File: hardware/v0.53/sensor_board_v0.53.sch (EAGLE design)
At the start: 55 parts, among them J3 USB-MICROB, U1 ATMEGA328P, U10 TSL2591, U3 OPA344, U4 RFM69HW, U5 FT231XS, U6 ADMP401, U7 SHT31-DIS, U8 MCP1703CB, U9 BMP280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

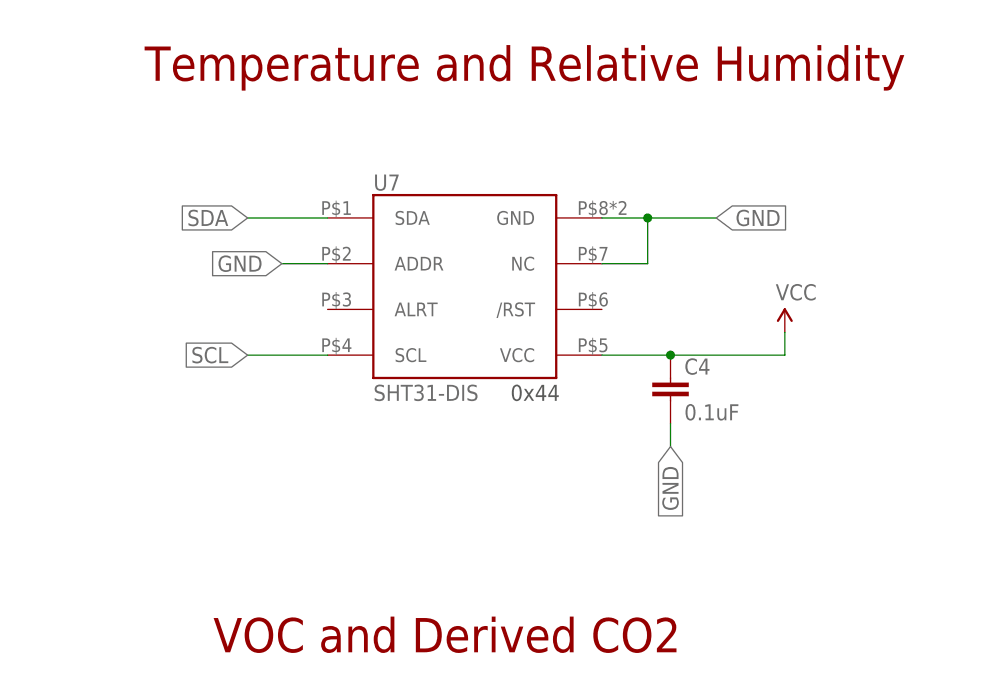
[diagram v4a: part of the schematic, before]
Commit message: Updated SHT31/35 library
Replaced old library with Adafruit version - slightly longer pads to avoid potential bridging during reflow.
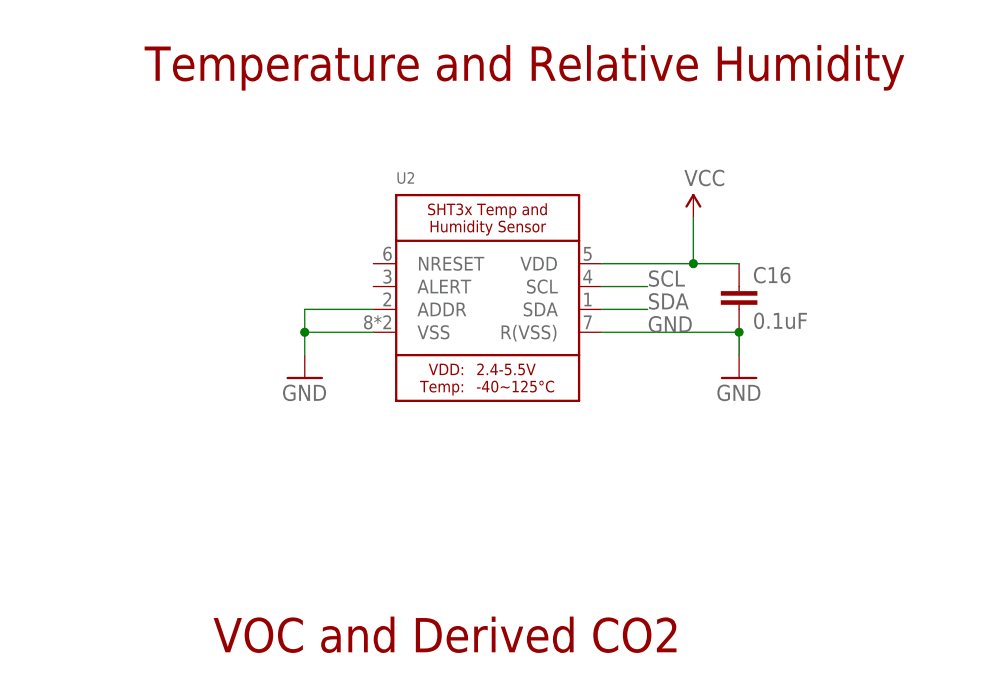
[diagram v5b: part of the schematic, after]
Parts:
- removed C4: 0.1uF, SparkFun-Passives:CAP0805
- removed U7: SHT31-DIS, thomasb9511:SHT31-DIS
- added C16: 0.1uF, SparkFun-Passives:CAP0805
- added U2: (no value), Adafruit SHT31:SHT3X
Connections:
- net GND: now also C16.2, U2.ADDR, U2.R(VSS), U2.VSS; no longer C4.2, U7.ADDR, U7.GND, U7.NC
- net SCL: now also U2.SCL; no longer U7.SCL
- net SDA: now also U2.SDA; no longer U7.SDA
- net VCC: now also C16.1, U2.VDD; no longer C4.1, U7.VCC
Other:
- note removed: "0x44"
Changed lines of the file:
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@@
 <attribute name="OC_NEWARK" value="58Y6083"/>
-</part>
-<part name="U7" library="thomasb9511" deviceset="SHT31-DIS" device="">
-<attribute name="MF" value=""/>
-<attribute name="MPN" value="SHT31-DIS-B"/>
-<attribute name="OC_NEWARK" value="47Y1304"/>
 </part>
 <part name="IAQ-CORE" library="IAQ-CORE" deviceset="IAQ-CORE" device="">
@@
 <part name="GND1" library="SparkFun-Aesthetics" deviceset="GND" device=""/>
 <part name="SUPPLY1" library="SparkFun-Aesthetics" deviceset="VCC" device=""/>
-<part name="SUPPLY3" library="SparkFun-Aesthetics" deviceset="VCC" device=""/>
 <part name="SUPPLY5" library="SparkFun-Aesthetics" deviceset="VCC" device=""/>
 <part name="R5" library="SparkFun-Resistors" deviceset="RESISTOR" device="0805-RES" value="10K">
@@
 <part name="R6" library="SparkFun-Resistors" deviceset="RESISTOR" device="0805-RES" value="10K">
 <attribute name="MPN" value="RC0805FR-0710KL"/>
-</part>
-<part name="C4" library="SparkFun-Passives" deviceset="CAP" device="0805" value="0.1uF">
-<attribute name="MPN" value="CC0805KRX7R9BB104"/>
 </part>
 <part name="C5" library="SparkFun-Passives" deviceset="CAP" device="0805" value="0.1uF">
@@
 <part name="J4" library="SparkFun-Connectors" deviceset="M02" device="PTH"/>
 <part name="J5" library="SparkFun-Connectors" deviceset="M02" device="PTH"/>
+<part name="U2" library="Adafruit SHT31" deviceset="SHT3X" device=""/>
+<part name="C16" library="SparkFun-Passives" deviceset="CAP" device="0805" value="0.1uF">
+<attribute name="MPN" value="CC0805KRX7R9BB104"/>
+</part>
+<part name="SUPPLY2" library="SparkFun-Aesthetics" deviceset="VCC" device=""/>
+<part name="GND8" library="SparkFun-Aesthetics" deviceset="GND" device=""/>
+<part name="GND13" library="SparkFun-Aesthetics" deviceset="GND" device=""/>
 </parts>
 <sheets>
@@
 <text x="-55.88" y="-45.72" size="3.81" layer="94">USB + FTDI</text>
 <text x="246.38" y="-78.74" size="1.778" layer="97">0x5A</text>
-<text x="248.92" y="-5.08" size="1.778" layer="97">0x44</text>
 <text x="157.48" y="12.7" size="1.778" layer="97">0x77</text>
 <text x="257.556" y="-102.362" size="2.54" layer="94" font="vector" ratio="10">0.53</text>
@@
 <attribute name="MPN" x="238.76" y="81.28" size="1.778" layer="96" rot="R270" display="off"/>
 </instance>
-<instance part="U7" gate="G$1" x="243.84" y="7.62">
-<attribute name="OC_NEWARK" x="243.84" y="7.62" size="1.778" layer="96" rot="R270" display="off"/>
-<attribute name="MF" x="243.84" y="7.62" size="1.778" layer="96" rot="R270" display="off"/>
-<attribute name="MPN" x="243.84" y="7.62" size="1.778" layer="96" rot="R270" display="off"/>
-</instance>
 <instance part="IAQ-CORE" gate="G$1" x="238.76" y="-59.69">
 <attribute name="OC_NEWARK" x="238.76" y="-59.69" size="1.778" layer="96" rot="R270" display="off"/>
@@
 <instance part="GND1" gate="1" x="208.28" y="48.26"/>
 <instance part="SUPPLY1" gate="G$1" x="208.28" y="127"/>
-<instance part="SUPPLY3" gate="G$1" x="279.4" y="2.54"/>
 <instance part="SUPPLY5" gate="G$1" x="269.24" y="-50.8"/>
 <instance part="R5" gate="G$1" x="274.32" y="109.22" rot="R90">
@@
 <instance part="R6" gate="G$1" x="284.48" y="109.22" rot="R90">
 <attribute name="MPN" x="284.48" y="109.22" size="1.778" layer="96" rot="R90" display="off"/>
-</instance>
-<instance part="C4" gate="G$1" x="266.7" y="-5.08">
-<attribute name="MPN" x="266.7" y="-5.08" size="1.778" layer="96" rot="R270" display="off"/>
 </instance>
 <instance part="C5" gate="G$1" x="269.24" y="-60.96">
@@
 <instance part="J4" gate="G$1" x="-10.16" y="-12.7"/>
 <instance part="J5" gate="G$1" x="20.32" y="-12.7"/>
+<instance part="U2" gate="G$1" x="246.38" y="7.62"/>
+<instance part="C16" gate="G$1" x="274.32" y="5.08">
+<attribute name="MPN" x="274.32" y="5.08" size="1.778" layer="96" rot="R270" display="off"/>
+</instance>
+<instance part="SUPPLY2" gate="G$1" x="269.24" y="15.24"/>
+<instance part="GND8" gate="1" x="274.32" y="-2.54"/>
+<instance part="GND13" gate="1" x="226.06" y="-2.54"/>
 </instances>
 <busses>
@@
 </segment>
 <segment>
-<pinref part="C4" gate="G$1" pin="2"/>
-<wire x1="266.7" y1="-7.62" x2="266.7" y2="-10.16" width="0.1524" layer="91"/>
-<label x="266.7" y="-10.16" size="1.778" layer="95" rot="R270" xref="yes"/>
-</segment>
-<segment>
-<pinref part="U7" gate="G$1" pin="GND"/>
-<wire x1="259.08" y1="15.24" x2="264.16" y2="15.24" width="0.1524" layer="91"/>
-<label x="271.78" y="15.24" size="1.778" layer="95" xref="yes"/>
-<pinref part="U7" gate="G$1" pin="NC"/>
-<wire x1="264.16" y1="15.24" x2="271.78" y2="15.24" width="0.1524" layer="91"/>
-<wire x1="259.08" y1="10.16" x2="264.16" y2="10.16" width="0.1524" layer="91"/>
-<wire x1="264.16" y1="10.16" x2="264.16" y2="15.24" width="0.1524" layer="91"/>
-<junction x="264.16" y="15.24"/>
-</segment>
-<segment>
-<pinref part="U7" gate="G$1" pin="ADDR"/>
-<wire x1="228.6" y1="10.16" x2="223.52" y2="10.16" width="0.1524" layer="91"/>
-<label x="223.52" y="10.16" size="1.778" layer="95" rot="R180" xref="yes"/>
-</segment>
-<segment>
 <pinref part="U9" gate="G$1" pin="GND"/>
 <wire x1="137.16" y1="17.78" x2="127" y2="17.78" width="0.1524" layer="91"/>
@@
 <wire x1="-2.54" y1="-12.7" x2="0" y2="-12.7" width="0.1524" layer="91"/>
 <label x="0" y="-12.7" size="1.778" layer="95"/>
+</segment>
+<segment>
+<pinref part="C16" gate="G$1" pin="2"/>
+<pinref part="GND8" gate="1" pin="GND"/>
+<wire x1="274.32" y1="2.54" x2="274.32" y2="0" width="0.1524" layer="91"/>
+<pinref part="U2" gate="G$1" pin="R(VSS)"/>
+<label x="264.16" y="2.54" size="1.778" layer="95"/>
+<wire x1="259.08" y1="2.54" x2="274.32" y2="2.54" width="0.1524" layer="91"/>
+<junction x="274.32" y="2.54"/>
+</segment>
+<segment>
+<pinref part="U2" gate="G$1" pin="VSS"/>
+<wire x1="233.68" y1="2.54" x2="226.06" y2="2.54" width="0.1524" layer="91"/>
+<pinref part="GND13" gate="1" pin="GND"/>
+<wire x1="226.06" y1="2.54" x2="226.06" y2="0" width="0.1524" layer="91"/>
+<pinref part="U2" gate="G$1" pin="ADDR"/>
+<wire x1="233.68" y1="5.08" x2="226.06" y2="5.08" width="0.1524" layer="91"/>
+<wire x1="226.06" y1="5.08" x2="226.06" y2="2.54" width="0.1524" layer="91"/>
+<junction x="226.06" y="2.54"/>
 </segment>
 </net>
@@
 </segment>
 <segment>
-<pinref part="U7" gate="G$1" pin="VCC"/>
-<wire x1="259.08" y1="0" x2="266.7" y2="0" width="0.1524" layer="91"/>
-<pinref part="C4" gate="G$1" pin="1"/>
-<pinref part="SUPPLY3" gate="G$1" pin="VCC"/>
-<wire x1="266.7" y1="0" x2="279.4" y2="0" width="0.1524" layer="91"/>
-<wire x1="279.4" y1="0" x2="279.4" y2="2.54" width="0.1524" layer="91"/>
-<junction x="266.7" y="0"/>
-</segment>
-<segment>
 <pinref part="U8" gate="G$1" pin="VO"/>
 <pinref part="C6" gate="G$1" pin="1"/>
@@
 <label x="0" y="-10.16" size="1.778" layer="95"/>
 </segment>
+<segment>
+<pinref part="U2" gate="G$1" pin="VDD"/>
+<pinref part="SUPPLY2" gate="G$1" pin="VCC"/>
+<wire x1="259.08" y1="10.16" x2="269.24" y2="10.16" width="0.1524" layer="91"/>
+<wire x1="269.24" y1="10.16" x2="269.24" y2="15.24" width="0.1524" layer="91"/>
+<pinref part="C16" gate="G$1" pin="1"/>
+<wire x1="269.24" y1="10.16" x2="274.32" y2="10.16" width="0.1524" layer="91"/>
+<junction x="269.24" y="10.16"/>
+</segment>
 </net>
 <net name="SCL" class="0">
@@
 </segment>
 <segment>
-<pinref part="U7" gate="G$1" pin="SCL"/>
-<wire x1="228.6" y1="0" x2="219.71" y2="0" width="0.1524" layer="91"/>
-<label x="219.71" y="0" size="1.778" layer="95" rot="R180" xref="yes"/>
-</segment>
-<segment>
 <pinref part="U9" gate="G$1" pin="SCK"/>
 <wire x1="167.64" y1="22.86" x2="170.18" y2="22.86" width="0.1524" layer="91"/>
@@
 <wire x1="-33.02" y1="-12.7" x2="-30.48" y2="-12.7" width="0.1524" layer="91"/>
 <label x="-30.48" y="-12.7" size="1.778" layer="95"/>
+</segment>
+<segment>
+<pinref part="U2" gate="G$1" pin="SCL"/>
+<wire x1="259.08" y1="7.62" x2="264.16" y2="7.62" width="0.1524" layer="91"/>
+<label x="264.16" y="7.62" size="1.778" layer="95"/>
 </segment>
 </net>
@@
 </segment>
 <segment>
-<pinref part="U7" gate="G$1" pin="SDA"/>
-<wire x1="228.6" y1="15.24" x2="219.71" y2="15.24" width="0.1524" layer="91"/>
-<label x="219.71" y="15.24" size="1.778" layer="95" rot="R180" xref="yes"/>
-</segment>
-<segment>
 <pinref part="IAQ-CORE" gate="G$1" pin="SDA"/>
 <wire x1="256.54" y1="-63.5" x2="259.08" y2="-63.5" width="0.1524" layer="91"/>
@@
 <label x="-30.48" y="-10.16" size="1.778" layer="95"/>
 </segment>
+<segment>
+<pinref part="U2" gate="G$1" pin="SDA"/>
+<wire x1="259.08" y1="5.08" x2="264.16" y2="5.08" width="0.1524" layer="91"/>
+<label x="264.16" y="5.08" size="1.778" layer="95"/>
+</segment>
 </net>

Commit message: Updated BOM
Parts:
- U2: MPN (none) -> SHT35-DIS-B
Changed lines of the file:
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@@
 </part>
 <part name="R3" library="SparkFun-Passives" deviceset="RESISTOR" device="0805-RES" value="1.5K">
-<attribute name="MPN" value="RC0805FR-071K5L
-"/>
+<attribute name="MPN" value="RC0805FR-071K5L "/>
 </part>
 <part name="R7" library="SparkFun-Passives" deviceset="RESISTOR" device="0805-RES" value="10K">
@@
 </part>
 <part name="R8" library="SparkFun-Passives" deviceset="RESISTOR" device="0805-RES" value="100K">
-<attribute name="MPN" value="RC0805FR-07100KL
-"/>
+<attribute name="MPN" value="RC0805FR-07100KL "/>
 </part>
 <part name="SUPPLY4" library="SparkFun-Aesthetics" deviceset="VCC" device=""/>
@@
 </part>
 <part name="R9" library="SparkFun-Passives" deviceset="RESISTOR" device="0805-RES" value="47">
-<attribute name="MPN" value="RC0805FR-0747RL
-"/>
+<attribute name="MPN" value="RC0805FR-0747RL "/>
 </part>
 <part name="R10" library="SparkFun-Passives" deviceset="RESISTOR" device="0805-RES" value="47">
-<attribute name="MPN" value="RC0805FR-0747RL
-"/>
+<attribute name="MPN" value="RC0805FR-0747RL "/>
 </part>
 <part name="R11" library="SparkFun-Passives" deviceset="RESISTOR" device="0805-RES" value="SHOTTKY">
@@
 </part>
 <part name="R12" library="SparkFun-Passives" deviceset="RESISTOR" device="0805-RES" value="27">
-<attribute name="MPN" value="RC0805FR-0727RL
-"/>
+<attribute name="MPN" value="RC0805FR-0727RL "/>
 </part>
 <part name="R21" library="SparkFun-Passives" deviceset="RESISTOR" device="0805-RES" value="27">
-<attribute name="MPN" value="RC0805FR-0727RL
-"/>
+<attribute name="MPN" value="RC0805FR-0727RL "/>
 </part>
 <part name="C11" library="SparkFun-Capacitors" deviceset="CAP" device="0805" value="0.1uF">
@@
 <part name="U$3" library="adafruit" deviceset="FIDUCIAL" device=""/>
 <part name="U10" library="TSL2591" deviceset="LIGHT_TSL2591" device="" value="TSL2591">
-<attribute name="MPN" value="TSL25911FN
-"/>
+<attribute name="MPN" value="TSL25911FN "/>
 </part>
 <part name="C14" library="SparkFun-Passives" deviceset="CAP" device="0805" value="0.1uF">
@@
 <part name="SUPPLY14" library="SparkFun-Aesthetics" deviceset="VCC" device=""/>
 <part name="R16" library="adafruit" deviceset="R-US_" device="R0603" value="470">
-<attribute name="MPN" value="RC0805FR-07470RL
-"/>
+<attribute name="MPN" value="RC0805FR-07470RL "/>
 </part>
 <part name="GND11" library="supply1" deviceset="GND" device=""/>
@@
 <part name="J4" library="SparkFun-Connectors" deviceset="M02" device="PTH"/>
 <part name="J5" library="SparkFun-Connectors" deviceset="M02" device="PTH"/>
-<part name="U2" library="Adafruit SHT31" deviceset="SHT3X" device=""/>
+<part name="U2" library="Adafruit SHT31" deviceset="SHT3X" device="">
+<attribute name="MPN" value="SHT35-DIS-B"/>
+</part>
 <part name="C16" library="SparkFun-Passives" deviceset="CAP" device="0805" value="0.1uF">
 <attribute name="MPN" value="CC0805KRX7R9BB104"/>
@@
 <instance part="J4" gate="G$1" x="-10.16" y="-12.7"/>
 <instance part="J5" gate="G$1" x="20.32" y="-12.7"/>
-<instance part="U2" gate="G$1" x="246.38" y="7.62"/>
+<instance part="U2" gate="G$1" x="246.38" y="7.62">
+<attribute name="MPN" x="246.38" y="7.62" size="1.778" layer="96" display="off"/>
+</instance>
 <instance part="C16" gate="G$1" x="274.32" y="5.08">
 <attribute name="MPN" x="274.32" y="5.08" size="1.778" layer="96" rot="R270" display="off"/>

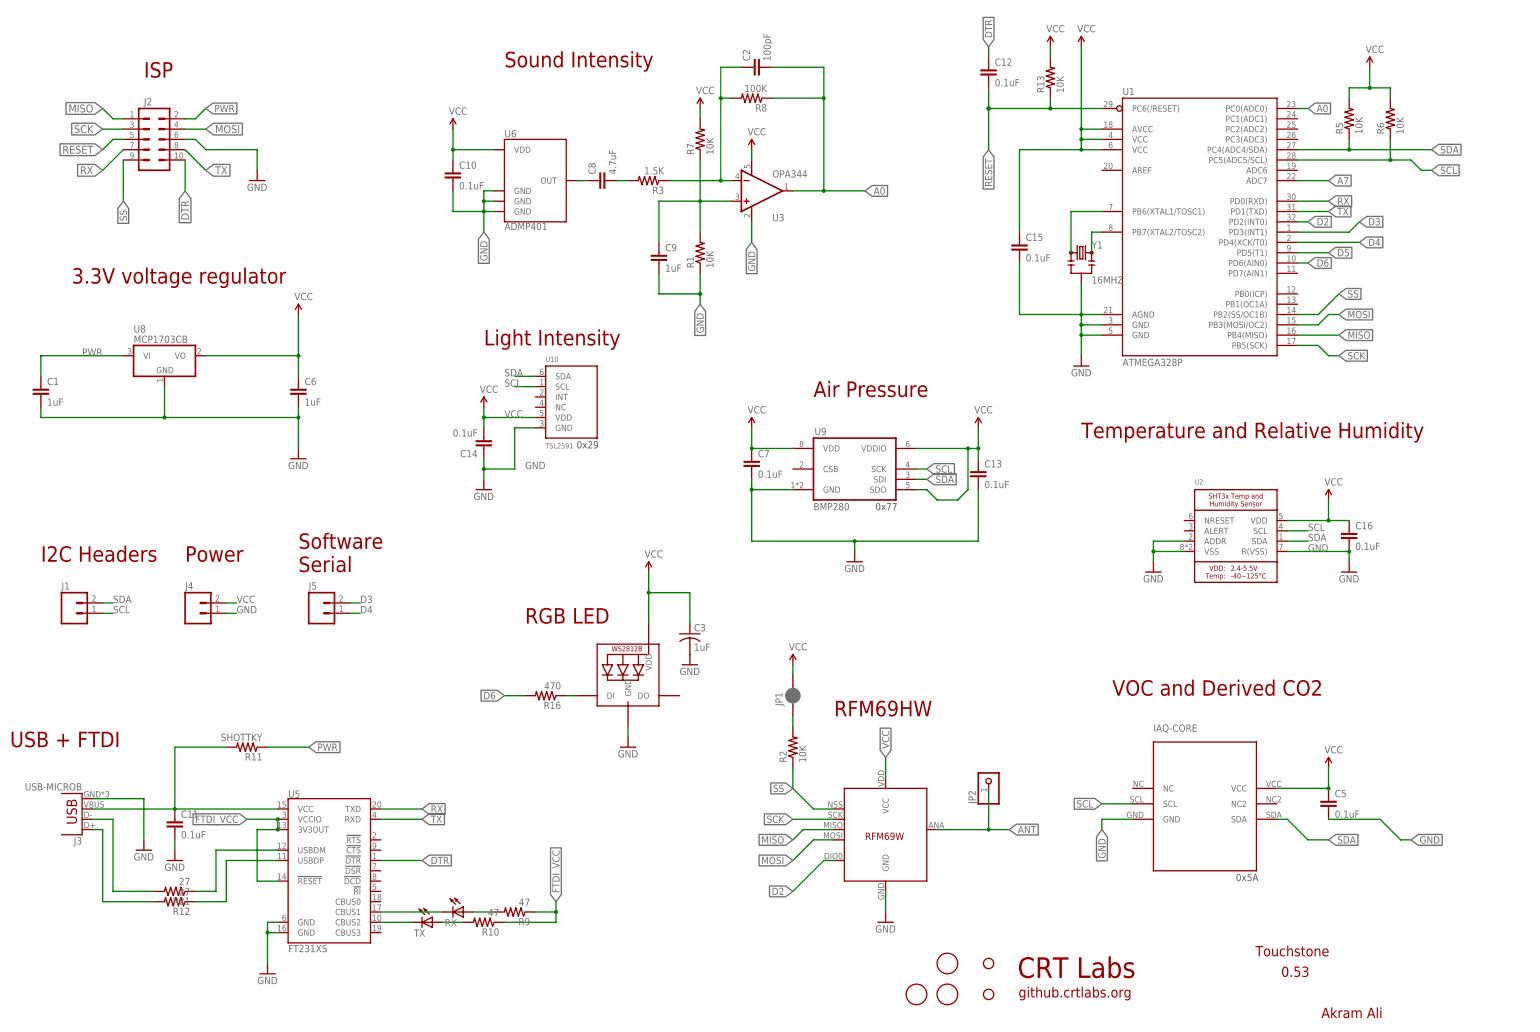
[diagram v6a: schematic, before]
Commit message: v0.53 - update
- Aligned light sensor with RGB LED
- Moved jumpers location after moving light sensor
- Added PM2.5 jumpers (RX/TX/PWR/GND)
- Adjusted some passive components
- Several trace adjustments
- Slightly increased board dimensions for added tolerance on mounting
holes
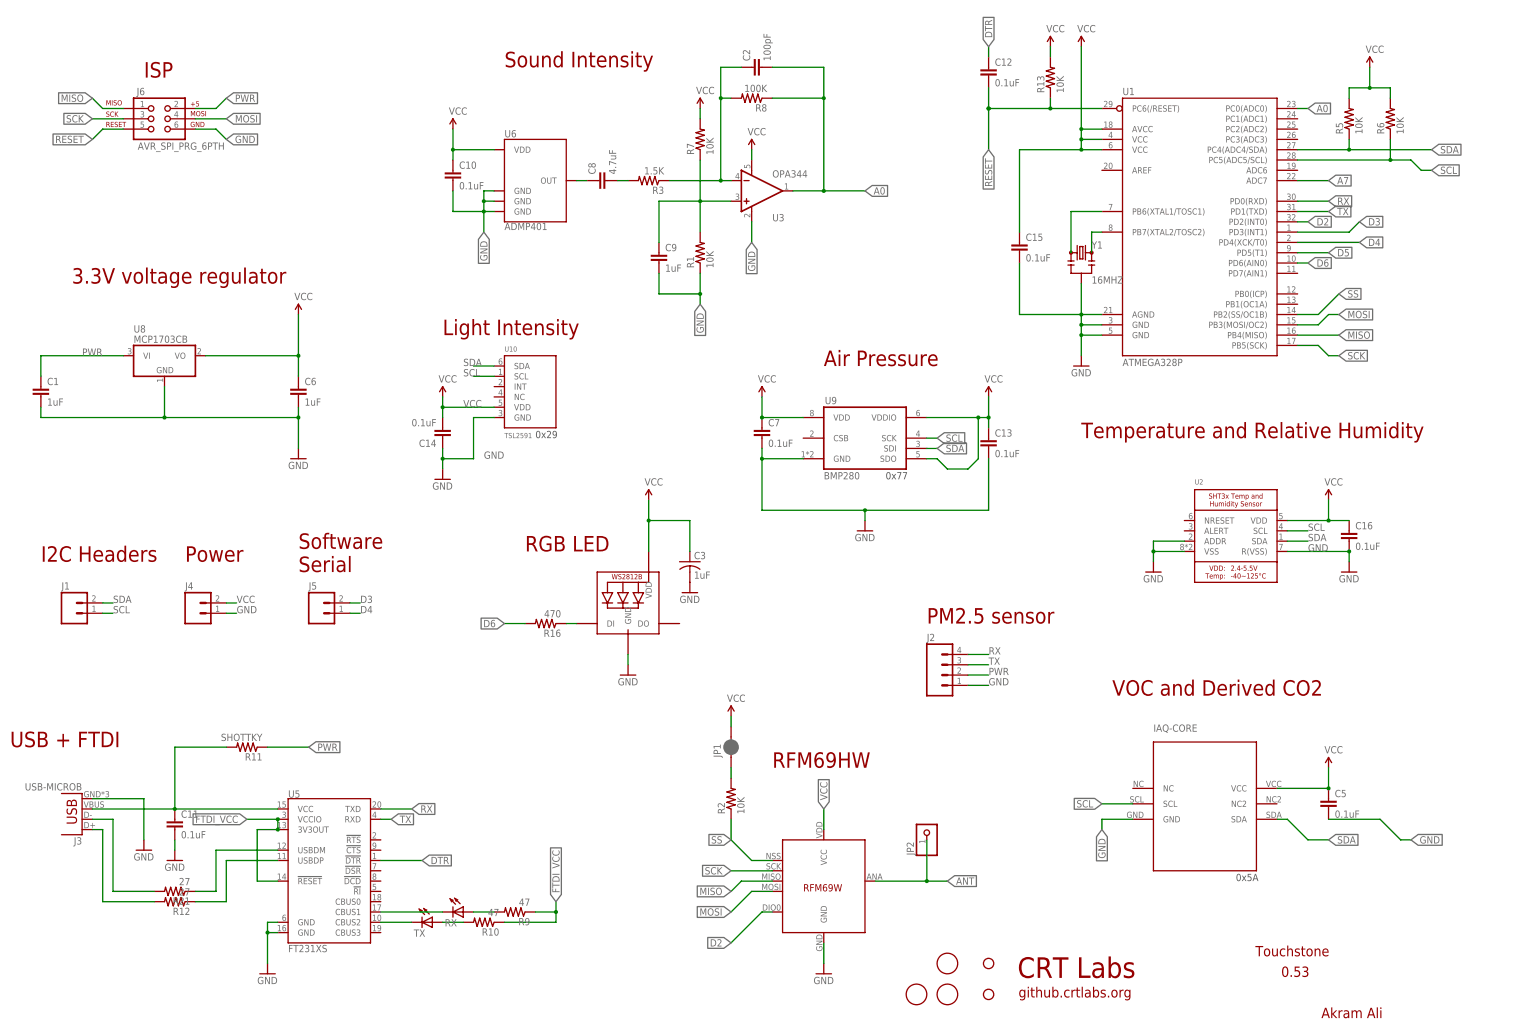
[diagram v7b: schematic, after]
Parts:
- added J6: AVR_SPI_PRG_6PTH, SparkFun-Connectors:AVR_SPI_PRG_6PTH
- J2: device SparkFun-Connectors:M05X2PTH -> SparkFun-Connectors:M04PTH
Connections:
- net DTR: no longer J2.10
- net GND: now also J2.1, J6.6; no longer J2.6
- net MISO: now also J6.1; no longer J2.1
- net MOSI: now also J6.4; no longer J2.4
- net PWR: now also J6.2
- net RESET: now also J6.5; no longer J2.5
- net RX: now also J2.4; no longer J2.7
- net SCK: now also J6.3; no longer J2.3
- net SS: no longer J2.9
- net TX: now also J2.3; no longer J2.8
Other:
- note added: "PM2.5 sensor"
- moved on the sheet: C13, C14, C3, C7, JP1, JP2, R16, R2, U10, U9
